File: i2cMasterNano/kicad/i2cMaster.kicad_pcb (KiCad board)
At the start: 2 copper layers, 27 parts, among them J1 Conn_01x04_Male, J10 Conn_01x01, J2 Conn_01x04_Male, J3 Conn_01x04_Male, J4 Conn_01x04_Male, J5 Conn_01x04_Male, J6 Conn_01x04_Male, J7 Conn_01x04_Male, J8 Conn_01x04_Male, J9 Conn_01x01, SW1 SW_DIP_x03, U1 LM7805_TO220, U2 Arduino_Nano_R3

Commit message: ...
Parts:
- moved U1 26.9 mm to (193.0, 121.9)
- moved C2 6.84 mm to (198.1, 86.4)
- moved TVS2 5.08 mm to (191.8, 74.9)
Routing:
- net Net-(C1-Pad1): track 91.2 -> 62.1 mm
- net +5V: track 229.3 -> 241.7 mm
- net GND: track 263.6 -> 260.4 mm
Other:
- net class Default: trace_width 1 -> 1.3
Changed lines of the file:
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@@
   (general
     (links 63)
-    (no_connects 1)
-    (area 129.064999 65.765 207.485001 165.230002)
+    (no_connects 2)
+    (area 129.064999 65.939999 207.485001 165.200001)
     (thickness 1.6)
     (drawings 6)
-    (tracks 165)
+    (tracks 163)
     (zones 0)
     (modules 27)
@@
   )
   (setup
-    (last_trace_width 1)
+    (last_trace_width 1.3)
     (user_trace_width 1)
     (user_trace_width 2)
@@
   (net_class Default "Toto je výchozí třída sítě."
     (clearance 0.4)
-    (trace_width 1)
+    (trace_width 1.3)
     (via_dia 0.6)
     (via_drill 0.4)
@@
   )
   (module TO_SOT_Packages_THT:TO-220-3_Vertical (layer F.Cu)
-    (at 196.85 95.25 90)
+    (at 193.04 121.92 90)
     (descr "TO-220-3, Vertical, RM 2.54mm")
     (tags "TO-220-3 Vertical RM 2.54mm")
@@
   )
   (module Capacitors_THT:CP_Radial_D10.0mm_P3.50mm (layer F.Cu)
-    (at 195.58 80.01)
+    (at 198.12 86.36)
     (descr "CP, Radial series, Radial, pin pitch=3.50mm, , diameter=10mm, Electrolytic Capacitor")
     (tags "CP Radial series Radial pin pitch 3.50mm  diameter 10mm Electrolytic Capacitor")
@@
   )
   (module Diodes_THT:D_5W_P12.70mm_Horizontal (layer F.Cu)
-    (at 191.77 69.85)
+    (at 191.77 74.93)
     (descr "D, 5W series, Axial, Horizontal, pin pitch=12.7mm, , length*diameter=8.9*3.7mm^2, , http://www.diodes.com/_files/packages/8686949.gif")
     (tags "D 5W series Axial Horizontal pin pitch 12.7mm  length 8.9mm diameter 3.7mm")
@@
   (gr_line (start 207.01 66.04) (end 207.01 111.76) (angle 90) (layer Margin) (width 0.2))
   (gr_line (start 129.54 163.83) (end 129.54 66.04) (angle 90) (layer Margin) (width 0.2))
+  (segment (start 193.04 119.38) (end 195.58 119.38) (width 1.3) (layer B.Cu) (net 1) (status 400000))
+  (segment (start 201.62 94.29) (end 201.62 86.36) (width 1.3) (layer B.Cu) (net 1) (status 800000))
+  (segment (start 196.85 99.06) (end 201.62 94.29) (width 1.3) (layer B.Cu) (net 1))
+  (segment (start 196.85 118.11) (end 196.85 99.06) (width 1.3) (layer B.Cu) (net 1))
+  (segment (start 195.58 119.38) (end 196.85 118.11) (width 1.3) (layer B.Cu) (net 1))
+  (segment (start 201.62 86.36) (end 203.2 86.36) (width 1.3) (layer B.Cu) (net 1) (status 400000))
+  (segment (start 203.2 86.36) (end 204.47 85.09) (width 1.3) (layer B.Cu) (net 1))
+  (segment (start 204.47 85.09) (end 204.47 74.93) (width 1.3) (layer B.Cu) (net 1) (status 800000))
+  (segment (start 189.23 119.38) (end 193.04 119.38) (width 1.3) (layer B.Cu) (net 1))
+  (segment (start 191.81 133.35) (end 191.81 130.85) (width 1.3) (layer B.Cu) (net 1))
+  (segment (start 189.23 111.76) (end 184.15 111.76) (width 1.3) (layer B.Cu) (net 1))
+  (segment (start 189.23 128.27) (end 189.23 119.38) (width 1.3) (layer B.Cu) (net 1))
+  (segment (start 189.23 119.38) (end 189.23 111.76) (width 1.3) (layer B.Cu) (net 1))
+  (segment (start 191.81 130.85) (end 189.23 128.27) (width 1.3) (layer B.Cu) (net 1))
   (segment (start 187.96 134.62) (end 189.23 133.35) (width 1.3) (layer B.Cu) (net 1))
-  (segment (start 199.08 80.01) (end 204.47 80.01) (width 1.3) (layer B.Cu) (net 1))
-  (segment (start 196.85 92.71) (end 201.93 92.71) (width 1.3) (layer B.Cu) (net 1))
-  (segment (start 204.47 90.17) (end 204.47 80.01) (width 1.3) (layer B.Cu) (net 1))
-  (segment (start 204.47 80.01) (end 204.47 69.85) (width 1.3) (layer B.Cu) (net 1))
-  (segment (start 201.93 92.71) (end 204.47 90.17) (width 1.3) (layer B.Cu) (net 1))
   (segment (start 191.81 133.35) (end 189.23 133.35) (width 1.3) (layer B.Cu) (net 1))
-  (segment (start 186.69 111.76) (end 191.81 111.76) (width 1.3) (layer B.Cu) (net 1))
-  (segment (start 191.81 111.76) (end 191.77 111.76) (width 1.3) (layer B.Cu) (net 1))
-  (segment (start 191.77 111.76) (end 191.81 111.76) (width 1.3) (layer B.Cu) (net 1))
-  (segment (start 196.85 92.71) (end 194.31 92.71) (width 1.3) (layer B.Cu) (net 1))
-  (segment (start 194.31 92.71) (end 191.81 95.21) (width 1.3) (layer B.Cu) (net 1))
-  (segment (start 191.81 95.21) (end 191.81 111.76) (width 1.3) (layer B.Cu) (net 1))
-  (segment (start 191.81 111.76) (end 191.81 133.35) (width 1.3) (layer B.Cu) (net 1))
   (segment (start 195.58 140.97) (end 195.58 139.7) (width 1.3) (layer B.Cu) (net 1))
   (segment (start 195.58 139.7) (end 191.77 135.89) (width 1.3) (layer B.Cu) (net 1))
@@
   (segment (start 165.1 116.84) (end 168.91 116.84) (width 1.3) (layer B.Cu) (net 1) (status 20))
   (segment (start 163.83 115.57) (end 165.1 116.84) (width 1.3) (layer B.Cu) (net 1))
-  (segment (start 184.15 111.76) (end 186.69 111.76) (width 1.3) (layer B.Cu) (net 1) (status 10))
+  (segment (start 198.12 86.36) (end 194.31 86.36) (width 1.3) (layer B.Cu) (net 2) (status 400000))
+  (segment (start 193.04 87.63) (end 193.04 116.84) (width 1.3) (layer B.Cu) (net 2) (status 800000))
+  (segment (start 194.31 86.36) (end 193.04 87.63) (width 1.3) (layer B.Cu) (net 2))
   (segment (start 180.34 80.01) (end 180.34 74.93) (width 1.3) (layer B.Cu) (net 2))
   (segment (start 175.26 74.93) (end 180.34 74.93) (width 1.3) (layer B.Cu) (net 2))
   (segment (start 180.34 74.93) (end 191.77 74.93) (width 1.3) (layer B.Cu) (net 2))
-  (segment (start 195.58 80.01) (end 195.58 78.74) (width 1.3) (layer B.Cu) (net 2))
-  (segment (start 195.58 78.74) (end 191.77 74.93) (width 1.3) (layer B.Cu) (net 2))
-  (segment (start 191.77 74.93) (end 191.77 69.85) (width 1.3) (layer B.Cu) (net 2))
-  (segment (start 196.85 90.17) (end 196.85 85.09) (width 1.3) (layer B.Cu) (net 2))
-  (segment (start 195.58 83.82) (end 195.58 80.01) (width 1.3) (layer B.Cu) (net 2))
-  (segment (start 196.85 85.09) (end 195.58 83.82) (width 1.3) (layer B.Cu) (net 2))
-  (segment (start 195.58 80.32) (end 195.89 80.01) (width 1.3) (layer B.Cu) (net 2) (status 30))
-  (segment (start 195.58 80.32) (end 195.89 80.01) (width 1.3) (layer B.Cu) (net 2) (status 30))
-  (segment (start 195.58 80.32) (end 195.89 80.01) (width 1.3) (layer B.Cu) (net 2) (status 30))
+  (segment (start 191.77 74.93) (end 191.77 74.93) (width 1.3) (layer B.Cu) (net 2) (status 20))
+  (segment (start 198.12 86.67) (end 198.43 86.36) (width 1.3) (layer B.Cu) (net 2) (status 30))
+  (segment (start 198.12 86.67) (end 198.43 86.36) (width 1.3) (layer B.Cu) (net 2) (status 30))
+  (segment (start 198.12 86.67) (end 198.43 86.36) (width 1.3) (layer B.Cu) (net 2) (status 30))
   (segment (start 143.51 129.54) (end 143.51 119.38) (width 1.3) (layer B.Cu) (net 2))
   (segment (start 143.51 149.86) (end 143.51 147.32) (width 1.3) (layer B.Cu) (net 2))
@@
   (segment (start 176.53 128.27) (end 176.53 153.67) (width 1) (layer B.Cu) (net 4))
   (segment (start 180.34 124.46) (end 176.53 128.27) (width 1) (layer B.Cu) (net 4))
-  (segment (start 196.85 135.89) (end 196.85 133.35) (width 2) (layer B.Cu) (net 24))
-  (segment (start 194.31 133.35) (end 195.58 133.35) (width 2) (layer B.Cu) (net 24))
-  (segment (start 195.58 133.35) (end 196.85 133.35) (width 2) (layer B.Cu) (net 24))
-  (segment (start 196.85 95.25) (end 196.85 97.79) (width 2) (layer B.Cu) (net 24))
-  (segment (start 196.85 97.79) (end 196.85 132.08) (width 2) (layer B.Cu) (net 24))
-  (segment (start 196.85 132.08) (end 196.85 133.35) (width 2) (layer B.Cu) (net 24))
-  (segment (start 198.12 137.16) (end 199.39 138.43) (width 2) (layer B.Cu) (net 24))
-  (segment (start 191.77 160.02) (end 191.77 163.83) (width 2) (layer B.Cu) (net 24))
-  (segment (start 191.77 163.83) (end 199.39 163.83) (width 2) (layer B.Cu) (net 24))
-  (segment (start 199.39 163.83) (end 199.39 138.43) (width 2) (layer B.Cu) (net 24))
-  (segment (start 198.12 137.16) (end 196.85 135.89) (width 2) (layer B.Cu) (net 24))
+  (segment (start 191.77 162.56) (end 193.04 163.83) (width 1) (layer B.Cu) (net 24))
+  (segment (start 198.12 163.83) (end 199.39 162.56) (width 1) (layer B.Cu) (net 24))
+  (segment (start 196.85 135.89) (end 194.31 133.35) (width 1) (layer B.Cu) (net 24) (status 800000))
+  (segment (start 194.31 133.35) (end 194.31 123.19) (width 1) (layer B.Cu) (net 24))
+  (segment (start 194.31 123.19) (end 193.04 121.92) (width 1) (layer B.Cu) (net 24))
+  (segment (start 198.12 137.16) (end 199.39 138.43) (width 1) (layer B.Cu) (net 24))
+  (segment (start 191.77 160.02) (end 191.77 162.56) (width 1) (layer B.Cu) (net 24))
+  (segment (start 193.04 163.83) (end 198.12 163.83) (width 1) (layer B.Cu) (net 24))
+  (segment (start 199.39 162.56) (end 199.39 138.43) (width 1) (layer B.Cu) (net 24))
+  (segment (start 198.12 137.16) (end 196.85 135.89) (width 1) (layer B.Cu) (net 24))
   (segment (start 191.77 160.02) (end 191.77 153.67) (width 2) (layer B.Cu) (net 24))
   (segment (start 191.77 160.02) (end 191.77 158.75) (width 2) (layer B.Cu) (net 24) (status 30))
-  (segment (start 196.85 95.25) (end 196.85 95.25) (width 2) (layer B.Cu) (net 24) (status 30))
+  (segment (start 193.04 121.92) (end 193.04 121.92) (width 2) (layer B.Cu) (net 24) (status 30))
   (segment (start 154.94 125.73) (end 158.75 125.73) (width 1) (layer B.Cu) (net 25))
   (segment (start 161.29 115.57) (end 161.29 113.03) (width 1) (layer B.Cu) (net 25))

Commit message: ...
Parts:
- J1, J2, J3, J4, J5, J6, J7, J8: value Conn_01x04_Male -> (none)
- REF** (x2): value DIN_Drziak -> (none)

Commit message: ...
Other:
- board outline added: 77.5 x 99.1 mm
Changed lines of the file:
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@@
     (trace_min 0.2)
     (segment_width 0.2)
-    (edge_width 0.15)
+    (edge_width 0.2)
     (via_size 0.6)
     (via_drill 0.4)
@@
     )
   )
-  (gr_line (start 129.54 165.1) (end 207.01 165.1) (angle 90) (layer Margin) (width 0.2))
-  (gr_line (start 207.01 66.04) (end 129.54 66.04) (angle 90) (layer Margin) (width 0.2))
+  (gr_line (start 129.54 165.1) (end 207.01 165.1) (angle 90) (layer Edge.Cuts) (width 0.2))
+  (gr_line (start 207.01 66.04) (end 129.54 66.04) (angle 90) (layer Edge.Cuts) (width 0.2))
   (gr_line (start 129.54 165.1) (end 129.54 163.83) (angle 90) (layer Margin) (width 0.2))
-  (gr_line (start 207.01 111.76) (end 207.01 165.1) (angle 90) (layer Margin) (width 0.2))
-  (gr_line (start 207.01 66.04) (end 207.01 111.76) (angle 90) (layer Margin) (width 0.2))
-  (gr_line (start 129.54 163.83) (end 129.54 66.04) (angle 90) (layer Margin) (width 0.2))
+  (gr_line (start 207.01 111.76) (end 207.01 165.1) (angle 90) (layer Edge.Cuts) (width 0.2))
+  (gr_line (start 207.01 66.04) (end 207.01 111.76) (angle 90) (layer Edge.Cuts) (width 0.2))
+  (gr_line (start 129.54 163.83) (end 129.54 66.04) (angle 90) (layer Edge.Cuts) (width 0.2))
   (segment (start 193.04 119.38) (end 195.58 119.38) (width 1.3) (layer B.Cu) (net 1))
   (segment (start 201.62 94.29) (end 201.62 86.36) (width 1.3) (layer B.Cu) (net 1))

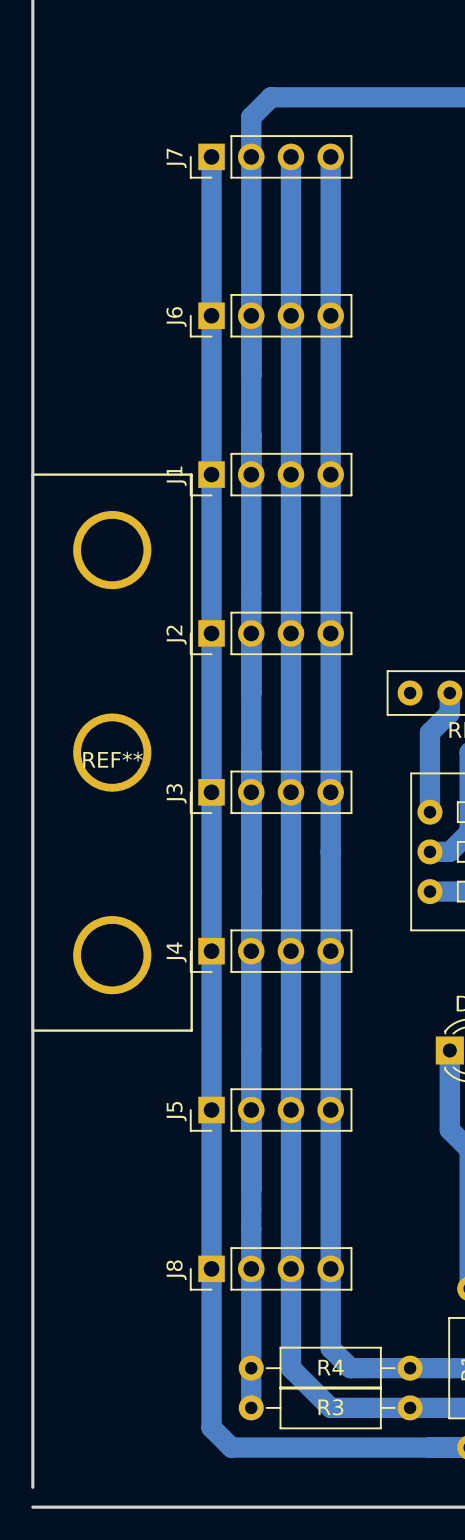
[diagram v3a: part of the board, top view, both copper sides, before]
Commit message: fixed 3d models for jst connectors and to220
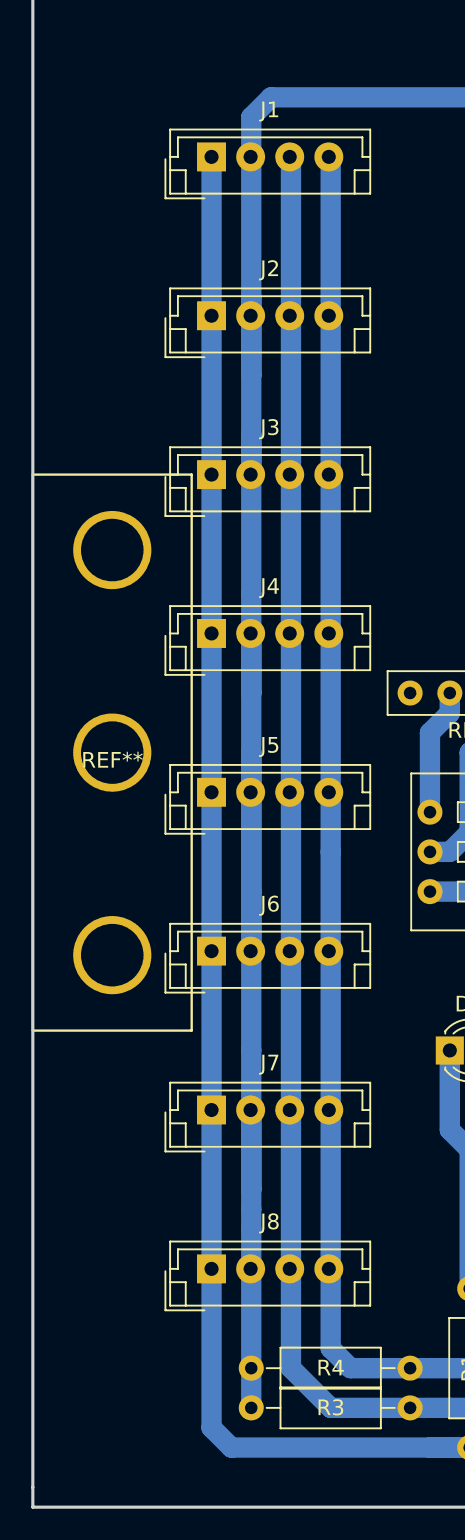
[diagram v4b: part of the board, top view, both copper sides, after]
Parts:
- J1: renamed from J7; value (none) -> Conn_01x04_Male; footprint Pin_Headers:Pin_Header_Straight_1x04_Pitch2.54mm -> Connectors_JST:JST_EH_B04B-EH-A_04x2.50mm_Straight
- J2: renamed from J6; value (none) -> Conn_01x04_Male; footprint Pin_Headers:Pin_Header_Straight_1x04_Pitch2.54mm -> Connectors_JST:JST_EH_B04B-EH-A_04x2.50mm_Straight
- J3: renamed from J1; value (none) -> Conn_01x04_Male; footprint Pin_Headers:Pin_Header_Straight_1x04_Pitch2.54mm -> Connectors_JST:JST_EH_B04B-EH-A_04x2.50mm_Straight
- J4: renamed from J2; value (none) -> Conn_01x04_Male; footprint Pin_Headers:Pin_Header_Straight_1x04_Pitch2.54mm -> Connectors_JST:JST_EH_B04B-EH-A_04x2.50mm_Straight
- J5: renamed from J3; value (none) -> Conn_01x04_Male; footprint Pin_Headers:Pin_Header_Straight_1x04_Pitch2.54mm -> Connectors_JST:JST_EH_B04B-EH-A_04x2.50mm_Straight
- J6: renamed from J4; value (none) -> Conn_01x04_Male; footprint Pin_Headers:Pin_Header_Straight_1x04_Pitch2.54mm -> Connectors_JST:JST_EH_B04B-EH-A_04x2.50mm_Straight
- J7: renamed from J5; value (none) -> Conn_01x04_Male; footprint Pin_Headers:Pin_Header_Straight_1x04_Pitch2.54mm -> Connectors_JST:JST_EH_B04B-EH-A_04x2.50mm_Straight
- J8: value (none) -> Conn_01x04_Male; footprint Pin_Headers:Pin_Header_Straight_1x04_Pitch2.54mm -> Connectors_JST:JST_EH_B04B-EH-A_04x2.50mm_Straight
- turned J1 to 0 degrees
- turned J2 to 0 degrees
- turned J3 to 0 degrees
- turned J4 to 0 degrees
- turned J5 to 0 degrees
- turned J6 to 0 degrees
- turned J7 to 0 degrees
- turned J8 to 0 degrees
